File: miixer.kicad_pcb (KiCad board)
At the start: 2 copper layers, 100 x 100 mm, 30 parts, among them J1 USB_C_Receptacle_USB2.0_16P, J2 Conn_01x10_Pin, SW2 SW_SPST, SW3 SW_SPST, SW4 SW_SPST, SW5 SW_SPST, SW6 SW_SPST, SW7 SW_SPST, SW8 SW_SPST, SW9 SW_SPST, U1 ESP32-C3-WROOM-02, U2 ADS1115IDGS, U3 USBLC6-2SC6, U4 AP2127K-3.3, U5 PCF8574T

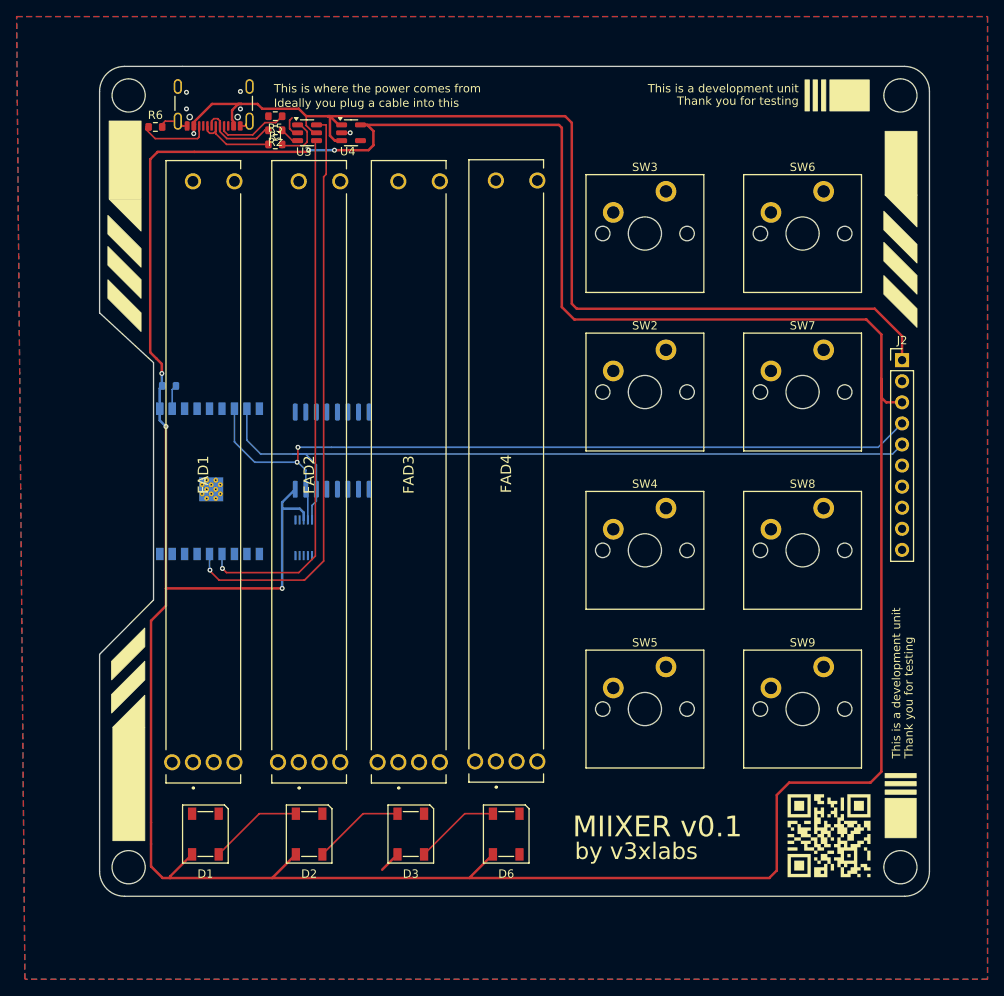
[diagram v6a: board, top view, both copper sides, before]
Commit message: Wire buttons
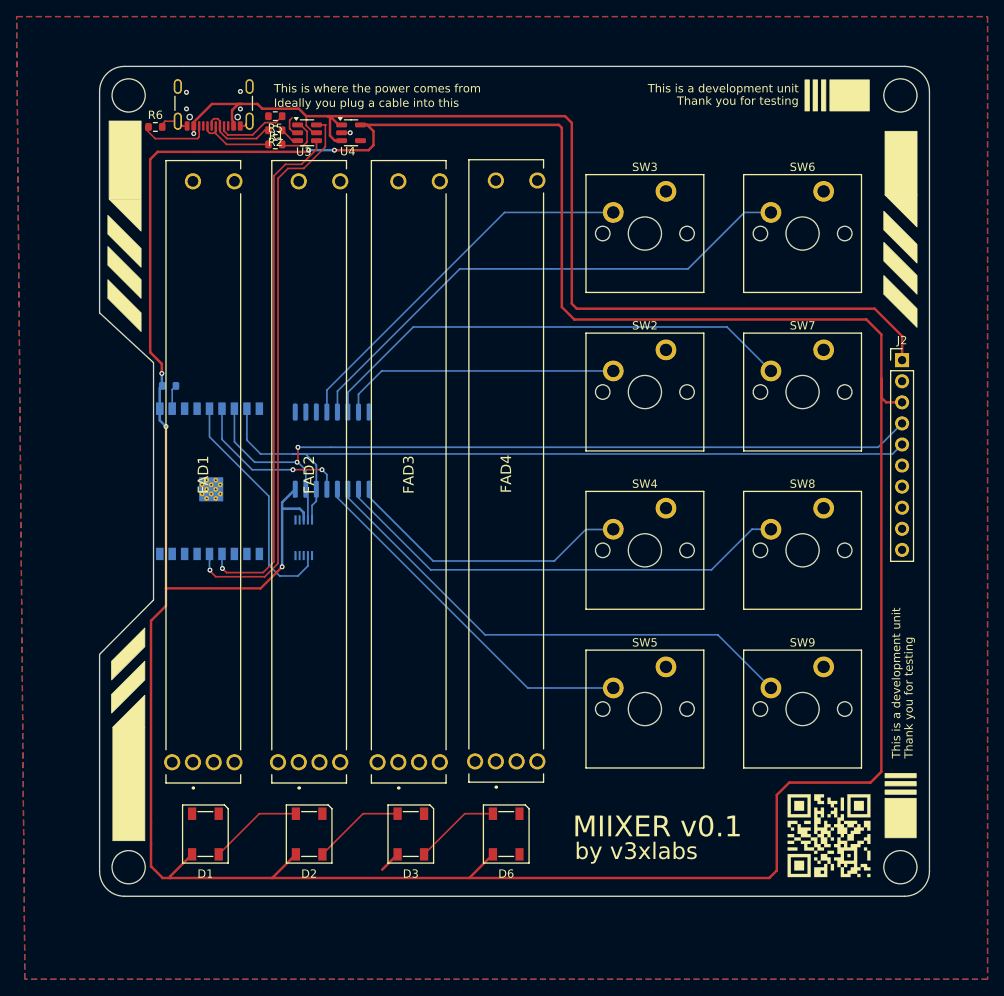
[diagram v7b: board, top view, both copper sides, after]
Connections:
- U1 pad 5: unconnected-(U1-IO6-Pad5) -> /Buttons/ADC_INTERRUPT
- U1 pad 6: unconnected-(U1-IO7-Pad6) -> /Buttons/BTN_INTERRUPT
- U2 pad 1: unconnected-(U2-ADDR-Pad1) -> GND
- U2 pad 2: unconnected-(U2-ALERT/RDY-Pad2) -> /Buttons/ADC_INTERRUPT
- U5 pad 1: unconnected-(U5-A0-Pad1) -> GND
- U5 pad 10: Net-(SW7-A) -> Net-(SW8-A)
- U5 pad 11: Net-(SW8-A) -> Net-(SW9-A)
- U5 pad 12: Net-(SW9-A) -> Net-(SW5-A)
- U5 pad 13: unconnected-(U5-~{INT}-Pad13) -> /Buttons/BTN_INTERRUPT
- U5 pad 2: unconnected-(U5-A1-Pad2) -> GND
- U5 pad 3: unconnected-(U5-A2-Pad3) -> GND
- U5 pad 5: Net-(SW2-A) -> Net-(SW6-A)
- U5 pad 6: Net-(SW4-A) -> Net-(SW7-A)
- U5 pad 7: Net-(SW5-A) -> Net-(SW2-A)
- U5 pad 9: Net-(SW6-A) -> Net-(SW4-A)
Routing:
- net Net-(SW6-A): track 0.00 -> 63.7 mm
- net Net-(SW9-A): track 0.00 -> 61.5 mm
- net Net-(SW7-A): track 0.00 -> 58.8 mm
- net Net-(SW8-A): track 0.00 -> 56.4 mm
- net Net-(SW3-A): track 0.00 -> 46.0 mm
- net Net-(SW5-A): track 0.00 -> 43.8 mm
- net Net-(SW4-A): track 0.00 -> 35.1 mm
- net Net-(SW2-A): track 0.00 -> 34.0 mm
- net /Buttons/ADC_INTERRUPT: track 0.00 -> 28.8 mm
- net /Buttons/BTN_INTERRUPT: track 0.00 -> 19.9 mm, vias 0 -> 2
- net /MCU/USB_D+: track 71.1 -> 68.8 mm
- net +3.3V: track 406.0 -> 404.5 mm
- net /MCU/USB_D-: track 64.1 -> 62.9 mm

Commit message: Update bom
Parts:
- U1: value ESP32-C3-WROOM-02 -> ESP32-C3-WROOM-02-N4
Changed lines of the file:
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@@
 		(sheetname "/Buttons/")
 		(sheetfile "schematics/buttons.kicad_sch")
-		(attr through_hole)
+		(attr through_hole exclude_from_bom dnp)
 		(fp_line
 			(start 72.5 -3.25)
@@
 		(sheetname "/Buttons/")
 		(sheetfile "schematics/buttons.kicad_sch")
-		(attr through_hole)
+		(attr through_hole exclude_from_bom dnp)
 		(fp_line
 			(start -7.1 -7.1)
@@
 		(sheetname "/Buttons/")
 		(sheetfile "schematics/buttons.kicad_sch")
-		(attr through_hole)
+		(attr through_hole exclude_from_bom dnp)
 		(fp_line
 			(start 72.5 -3.25)
@@
 		(sheetname "/Buttons/")
 		(sheetfile "schematics/buttons.kicad_sch")
-		(attr through_hole)
+		(attr through_hole exclude_from_bom dnp)
 		(fp_line
 			(start 72.5 -3.25)
@@
 		(sheetname "/Buttons/")
 		(sheetfile "schematics/buttons.kicad_sch")
-		(attr through_hole)
+		(attr through_hole exclude_from_bom dnp)
 		(fp_line
 			(start -7.1 -7.1)
@@
 		(sheetname "/Buttons/")
 		(sheetfile "schematics/buttons.kicad_sch")
-		(attr through_hole)
+		(attr through_hole exclude_from_bom dnp)
 		(fp_line
 			(start -7.1 -7.1)
@@
 		(sheetname "/Buttons/")
 		(sheetfile "schematics/buttons.kicad_sch")
-		(attr through_hole)
+		(attr through_hole exclude_from_bom dnp)
 		(fp_line
 			(start -7.1 -7.1)
@@
 			)
 		)
+		(attr exclude_from_bom dnp)
 		(fp_rect
 			(start -5 -5)
@@
 		(sheetname "/Buttons/")
 		(sheetfile "schematics/buttons.kicad_sch")
-		(attr through_hole)
+		(attr through_hole exclude_from_bom dnp)
 		(fp_line
 			(start 72.5 -3.25)
@@
 		(sheetname "/Buttons/")
 		(sheetfile "schematics/buttons.kicad_sch")
-		(attr through_hole)
+		(attr through_hole exclude_from_bom dnp)
 		(fp_line
 			(start -7.1 -7.1)
@@
 		(sheetname "/Buttons/")
 		(sheetfile "schematics/buttons.kicad_sch")
-		(attr through_hole)
+		(attr through_hole exclude_from_bom dnp)
 		(fp_line
 			(start -7.1 -7.1)
@@
 		(sheetname "/Buttons/")
 		(sheetfile "schematics/buttons.kicad_sch")
-		(attr through_hole)
+		(attr through_hole exclude_from_bom dnp)
 		(fp_line
 			(start -7.1 -7.1)
@@
 		(sheetname "/Buttons/")
 		(sheetfile "schematics/buttons.kicad_sch")
-		(attr through_hole)
+		(attr through_hole exclude_from_bom dnp)
 		(fp_line
 			(start -7.1 -7.1)
@@
 		(sheetname "/")
 		(sheetfile "miixer.kicad_sch")
-		(attr through_hole)
+		(attr through_hole exclude_from_bom dnp)
 		(fp_line
 			(start -1.38 -1.38)
@@
 		(embedded_fonts no)
 		(model "${KICAD9_3DMODEL_DIR}/Connector_PinHeader_2.54mm.3dshapes/PinHeader_1x10_P2.54mm_Vertical.step"
+			(hide yes)
 			(offset
 				(xyz 0 0 0)
@@
 			)
 		)
-		(property "Value" "ESP32-C3-WROOM-02"
+		(property "Value" "ESP32-C3-WROOM-02-N4"
 			(at 6.6 -3.375 90)
 			(layer "B.Fab")
